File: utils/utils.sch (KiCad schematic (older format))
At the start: 25 parts, among them J1 AIN, J2 BIN, J3 GATE, J4 EURORACK_CONN_10, J5 ~OUT, J6 OUT, J7 Conn_01x04, J8 Conn_01x05, Q1 2N3904, U1 TL072, U2 4066, U3 LM317L_TO92, U4 LM337L_TO92

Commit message: rework PCB
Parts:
- added J9: Conn_01x03_Male, 4ms/4ms-kicad-lib/4ms-footprints.pretty:Pin_Header_Straight_1x03, symbol Connector:Conn_01x03_Male
- added JP1, JP2, JP3, JP4, JP5, JP6, JP7, JP8, JP9: Jumper_2_Open, fruchti/fruchtilib/mod/rcl.pretty:SOLDER_JUMPER_0603_B, symbol Jumper:Jumper_2_Open
- D1: footprint (none) -> 4ms/4ms-kicad-lib/4ms-footprints.pretty:LED-3MM-SQUARE-ANODE
- J7: footprint imciner2/KiCad-Libraries/modules/Connectors.pretty:CONN_2.54mm_1x04 -> imciner2/KiCad-Libraries/modules/Connectors.pretty:CONN_2.54mm_1x05
- Q1: footprint Package_TO_SOT_THT:TO-92_Inline -> 4ms/4ms-kicad-lib/lib-footprints/4ms_Package_TO.pretty:TO-92_OffsetPin2
- R10, R11: footprint (none) -> 4ms/4ms-kicad-lib/4ms-footprints.pretty:Resistor_TH_300
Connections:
- net labels added: STAGE1_OUT
- wire segments 146 -> 172
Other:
- note added: "This is a trick to only use the LED to show gate state\nif the GATE jack is used. When jack is unplugged,\nGATE_CONN is grounded, turning off the transistor.\nWhen jack is plugged, GATE_CONN floats, allowing\nthe gate to control the transistor. R10 gives an input\nimpedance of 100K, since LED is driven by power\nsupply. LED on current depends on GATE but maxes\nabout 4mA"
- note removed: "This is a trick to only use the LED to show gate state\nif the GATE jack is used. When jack is unplugged,\nGATE_CONN is grounded, turning off the transistor.\nWhen jack is plugged, GATE_CONN floats, allowing\nthe gate to control the transistor. R10 gives an input\nimpedance of 100K, since LED is driven by power\nsupply. LED on current about 4mA\n\nTODO: is this enough current? does the slow turn-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"
- moved on the sheet: D1, J7, J8, Q1, R1, R10, R11, R2, R4, R5, U1A, U1B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

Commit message: use through-holes for pot
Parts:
- RV1: footprint rdeterre/misc.pretty:Potentiometer_Bourns_PDB182-K_Dual -> imciner2/KiCad-Libraries/modules/Connectors.pretty:CONN_2.54mm_1x03
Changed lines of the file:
@@
 F 0 "RV1" V 3543 1950 50  0000 C CNN
 F 1 "200K" V 3634 1950 50  0000 C CNN
-F 2 "rdeterre/misc.pretty:Potentiometer_Bourns_PDB182-K_Dual" H 3750 1950 50  0001 C CNN
+F 2 "imciner2/KiCad-Libraries/modules/Connectors.pretty:CONN_2.54mm_1x03" H 3750 1950 50  0001 C CNN
 F 3 "~" H 3750 1950 50  0001 C CNN
 	1    3750 1950

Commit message: add support for fixed CV output when no input
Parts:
- removed RV1: 200K, imciner2/KiCad-Libraries/modules/Connectors.pretty:CONN_2.54mm_1x03, symbol Device:R_POT
- added R12, R3: 10K, 4ms/4ms-kicad-lib/4ms-footprints.pretty:Resistor_TH_300, symbol Device:R
- added RV1: 200K, 4ms/4ms-kicad-lib/4ms-footprints.pretty:Pin_Header_Straight_2x03_Pitch2.54mm, symbol Device:R_POT_Dual_Separate
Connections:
- net labels added: A_CONN
- wire segments 172 -> 178
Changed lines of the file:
@@
 	1    0    0    -1
 $EndComp
-$Comp
-L Device:R R1
-U 1 1 5ECB39F0
-P 2950 2100
-F 0 "R1" V 2743 2100 50  0000 C CNN
-F 1 "100K" V 2834 2100 50  0000 C CNN
-F 2 "4ms/4ms-kicad-lib/4ms-footprints.pretty:Resistor_TH_300" V 2880 2100 50  0001 C CNN
-F 3 "~" H 2950 2100 50  0001 C CNN
-	1    2950 2100
-	0    1    1    0
-$EndComp
-$Comp
-L Device:R R2
-U 1 1 5ECB414F
-P 2950 2400
-F 0 "R2" V 2743 2400 50  0000 C CNN
-F 1 "100K" V 2834 2400 50  0000 C CNN
-F 2 "4ms/4ms-kicad-lib/4ms-footprints.pretty:Resistor_TH_300" V 2880 2400 50  0001 C CNN
-F 3 "~" H 2950 2400 50  0001 C CNN
-	1    2950 2400
-	0    1    1    0
-$EndComp
-$Comp
-L power:GND #PWR05
-U 1 1 5ECB8733
-P 3250 2700
-F 0 "#PWR05" H 3250 2450 50  0001 C CNN
-F 1 "GND" H 3255 2527 50  0000 C CNN
-F 2 "" H 3250 2700 50  0001 C CNN
-F 3 "" H 3250 2700 50  0001 C CNN
-	1    3250 2700
-	1    0    0    -1
-$EndComp
-Wire Wire Line
-	3250 2700 3250 2600
-Wire Wire Line
-	3250 2600 3350 2600
 Wire Wire Line
 	3100 2400 3150 2400
@@
 	900  1550 900  1500
 Wire Wire Line
-	1100 950  1200 950
-Wire Wire Line
-	1200 950  1200 1050
-Wire Wire Line
 	1200 1500 900  1500
 Connection ~ 900  1500
@@
 	900  1500 900  1450
 Wire Wire Line
-	1100 1050 1200 1050
-Connection ~ 1200 1050
-Wire Wire Line
-	1200 1050 1200 1250
-Wire Wire Line
 	1100 1250 1200 1250
-Connection ~ 1200 1250
 Wire Wire Line
 	1200 1250 1200 1500
@@
 	900  2700 900  2650
 Wire Wire Line
-	1100 2100 1200 2100
-Wire Wire Line
-	1200 2100 1200 2200
-Wire Wire Line
 	1200 2650 900  2650
 Connection ~ 900  2650
@@
 	900  2650 900  2600
 Wire Wire Line
-	1100 2200 1200 2200
-Connection ~ 1200 2200
-Wire Wire Line
-	1200 2200 1200 2400
-Wire Wire Line
 	1100 2400 1200 2400
-Connection ~ 1200 2400
 Wire Wire Line
 	1200 2400 1200 2650
@@
 Text Notes 8150 3600 0    50   ~ 0
 The CD4066 has a max power supply voltage of 20V,\nso we step the 24V down to about 19.5 via regulators.\nIn theory we could hacky do this with 6 diodes instead.\n\nBy limiting TL072 to the same supply, we don’t risk over-volting\nthe 4066, because even at rail  outputs the 4066 is safe.
-$Comp
-L Device:R_POT RV1
-U 1 1 5ECB664B
-P 3750 1950
-F 0 "RV1" V 3543 1950 50  0000 C CNN
-F 1 "200K" V 3634 1950 50  0000 C CNN
-F 2 "imciner2/KiCad-Libraries/modules/Connectors.pretty:CONN_2.54mm_1x03" H 3750 1950 50  0001 C CNN
-F 3 "~" H 3750 1950 50  0001 C CNN
-	1    3750 1950
-	0    1    1    0
-$EndComp
 Wire Wire Line
 	3300 1950 3300 2400
@@
 Wire Wire Line
 	8300 5350 8400 5350
+$Comp
+L Device:R_POT_Dual_Separate RV1
+U 2 1 5ED32DF1
+P 3750 1950
+F 0 "RV1" V 3543 1950 50  0000 C CNN
+F 1 "200K" V 3634 1950 50  0000 C CNN
+F 2 "4ms/4ms-kicad-lib/4ms-footprints.pretty:Pin_Header_Straight_2x03_Pitch2.54mm" H 3750 1950 50  0001 C CNN
+F 3 "~" H 3750 1950 50  0001 C CNN
+	2    3750 1950
+	0    1    1    0
+$EndComp
+$Comp
+L Device:R_POT_Dual_Separate RV1
+U 1 1 5ED34631
+P 2800 3400
+F 0 "RV1" H 2731 3446 50  0000 R CNN
+F 1 "200K" H 2731 3355 50  0000 R CNN
+F 2 "4ms/4ms-kicad-lib/4ms-footprints.pretty:Pin_Header_Straight_2x03_Pitch2.54mm" H 2800 3400 50  0001 C CNN
+F 3 "~" H 2800 3400 50  0001 C CNN
+	1    2800 3400
+	1    0    0    -1
+$EndComp
+$Comp
+L Device:R R2
+U 1 1 5ECB414F
+P 2950 2400
+F 0 "R2" V 2743 2400 50  0000 C CNN
+F 1 "100K" V 2834 2400 50  0000 C CNN
+F 2 "4ms/4ms-kicad-lib/4ms-footprints.pretty:Resistor_TH_300" V 2880 2400 50  0001 C CNN
+F 3 "~" H 2950 2400 50  0001 C CNN
+	1    2950 2400
+	0    1    1    0
+$EndComp
+$Comp
+L Device:R R1
+U 1 1 5ECB39F0
+P 2950 2100
+F 0 "R1" V 2743 2100 50  0000 C CNN
+F 1 "100K" V 2834 2100 50  0000 C CNN
+F 2 "4ms/4ms-kicad-lib/4ms-footprints.pretty:Resistor_TH_300" V 2880 2100 50  0001 C CNN
+F 3 "~" H 2950 2100 50  0001 C CNN
+	1    2950 2100
+	0    1    1    0
+$EndComp
+$Comp
+L power:+10V #PWR0101
+U 1 1 5ED62298
+P 2800 2800
+F 0 "#PWR0101" H 2800 2650 50  0001 C CNN
+F 1 "+10V" H 2815 2973 50  0000 C CNN
+F 2 "" H 2800 2800 50  0001 C CNN
+F 3 "" H 2800 2800 50  0001 C CNN
+	1    2800 2800
+	1    0    0    -1
+$EndComp
+$Comp
+L power:-10V #PWR0102
+U 1 1 5EDA3B1B
+P 2800 4000
+F 0 "#PWR0102" H 2800 4100 50  0001 C CNN
+F 1 "-10V" H 2815 4173 50  0000 C CNN
+F 2 "" H 2800 4000 50  0001 C CNN
+F 3 "" H 2800 4000 50  0001 C CNN
+	1    2800 4000
+	-1   0    0    1
+$EndComp
+Wire Wire Line
+	2950 3400 3100 3400
+Wire Wire Line
+	3100 3400 3100 2600
+Wire Wire Line
+	3100 2600 3350 2600
+Wire Wire Line
+	2800 2800 2800 2900
+Wire Wire Line
+	2800 3250 2800 3200
+$Comp
+L Device:R R3
+U 1 1 5ED35BE2
+P 2800 3050
+F 0 "R3" V 2593 3050 50  0000 C CNN
+F 1 "10K" V 2684 3050 50  0000 C CNN
+F 2 "4ms/4ms-kicad-lib/4ms-footprints.pretty:Resistor_TH_300" V 2730 3050 50  0001 C CNN
+F 3 "~" H 2800 3050 50  0001 C CNN
+	1    2800 3050
+	-1   0    0    1
+$EndComp
+Wire Wire Line
+	2800 4000 2800 3900
+Wire Wire Line
+	2800 3600 2800 3550
+$Comp
+L Device:R R12
+U 1 1 5ED360F9
+P 2800 3750
+F 0 "R12" V 2593 3750 50  0000 C CNN
+F 1 "10K" V 2684 3750 50  0000 C CNN
+F 2 "4ms/4ms-kicad-lib/4ms-footprints.pretty:Resistor_TH_300" V 2730 3750 50  0001 C CNN
+F 3 "~" H 2800 3750 50  0001 C CNN
+	1    2800 3750
+	-1   0    0    1
+$EndComp
+Wire Wire Line
+	1100 2100 1200 2100
+Wire Wire Line
+	1100 2200 1200 2200
+Wire Wire Line
+	1200 2100 1200 2200
+Connection ~ 1200 2400
+Connection ~ 1200 2200
+Wire Wire Line
+	1200 2200 1200 2400
+Text GLabel 1450 950  2    50   Input ~ 0
+A_CONN
+Wire Wire Line
+	1450 950  1200 950
+Text GLabel 3250 3400 2    50   Input ~ 0
+A_CONN
+Wire Wire Line
+	3250 3400 3100 3400
+Connection ~ 3100 3400
+Wire Wire Line
+	1100 1050 1200 1050
+Wire Wire Line
+	1200 1050 1200 950
+Connection ~ 1200 950
+Wire Wire Line
+	1200 950  1100 950
 $EndSCHEMATC

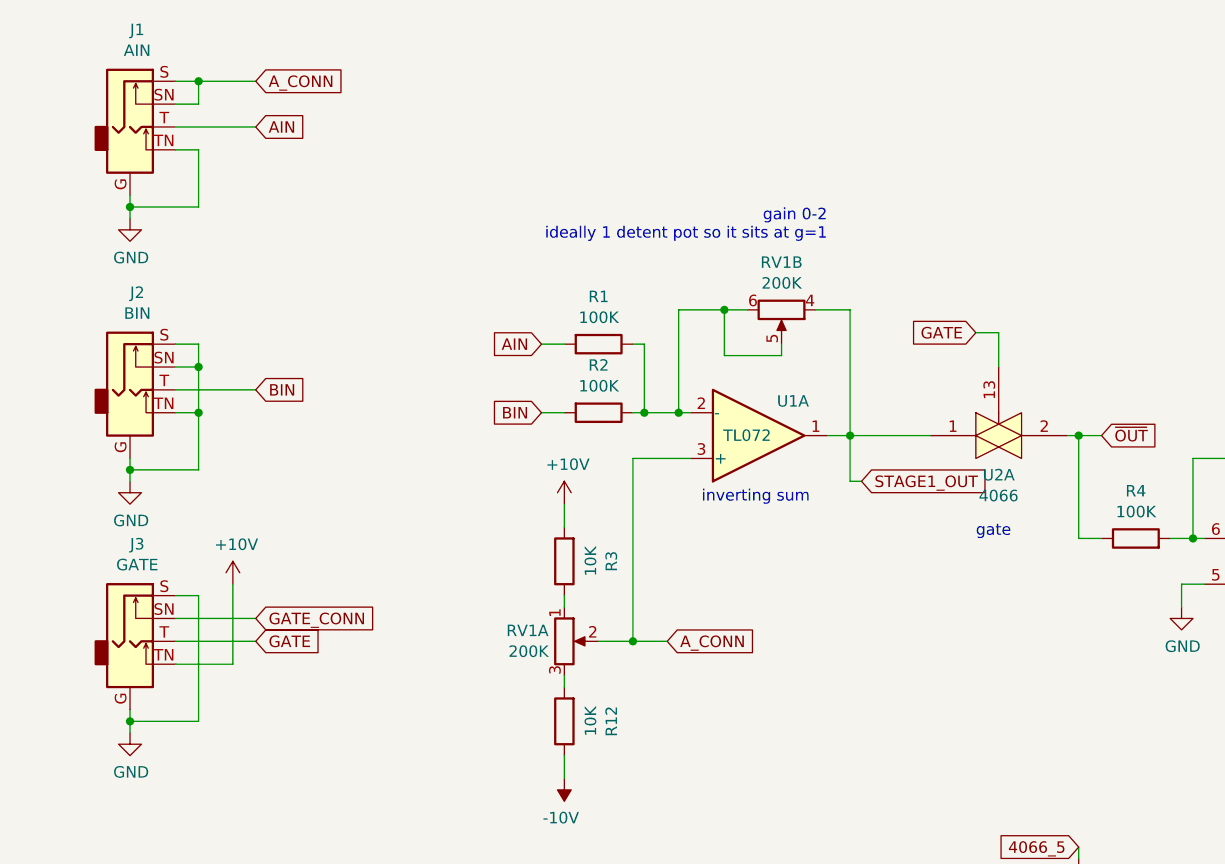
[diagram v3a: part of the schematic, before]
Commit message: correction based on breadboard test
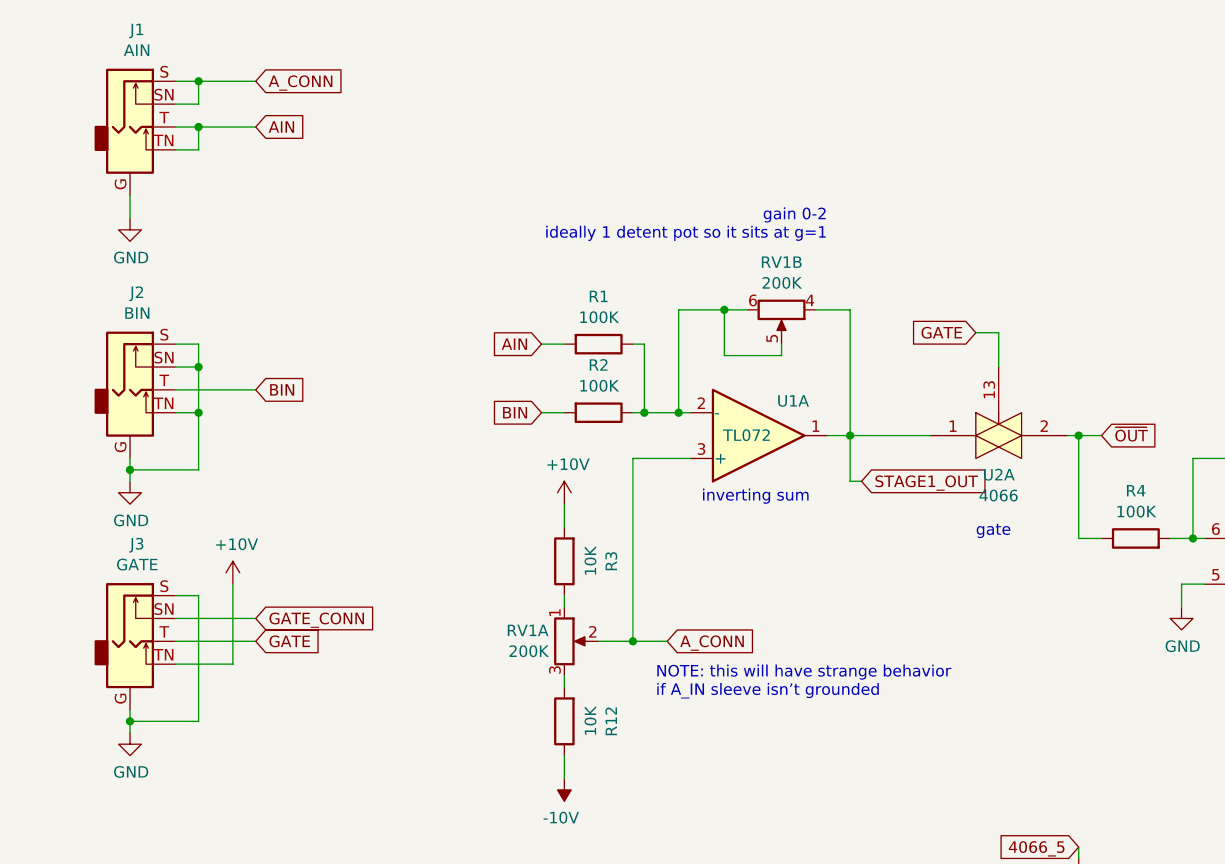
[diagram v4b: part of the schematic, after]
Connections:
- net AIN: now also J1.TN
- net GND: no longer J1.TN
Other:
- note added: "NOTE: this will have strange behavior\nif A_IN sleeve isn’t grounded"
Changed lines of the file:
@@
 	1    0    0    -1
 $EndComp
-Wire Wire Line
-	900  1550 900  1500
-Wire Wire Line
-	1200 1500 900  1500
-Connection ~ 900  1500
-Wire Wire Line
-	900  1500 900  1450
-Wire Wire Line
-	1100 1250 1200 1250
-Wire Wire Line
-	1200 1250 1200 1500
 Text GLabel 1450 1150 2    50   Input ~ 0
 AIN
 Wire Wire Line
-	1450 1150 1100 1150
+	1450 1150 1200 1150
 $Comp
 L synth:AudioJack2_Ground_Switch J2
@@
 Wire Wire Line
 	1200 950  1100 950
+Wire Wire Line
+	900  1450 900  1550
+Wire Wire Line
+	1100 1250 1200 1250
+Wire Wire Line
+	1200 1250 1200 1150
+Connection ~ 1200 1150
+Wire Wire Line
+	1200 1150 1100 1150
+Text Notes 3200 3650 0    50   ~ 0
+NOTE: this will have strange behavior\nif A_IN sleeve isn’t grounded
 $EndSCHEMATC

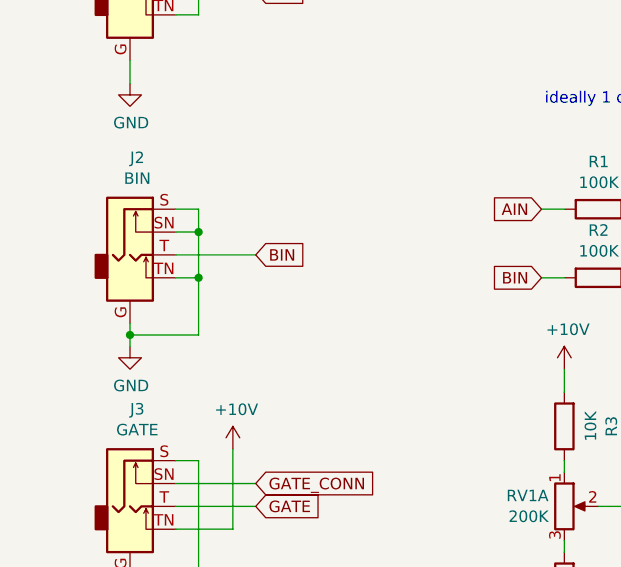
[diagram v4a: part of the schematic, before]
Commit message: correct ground issue
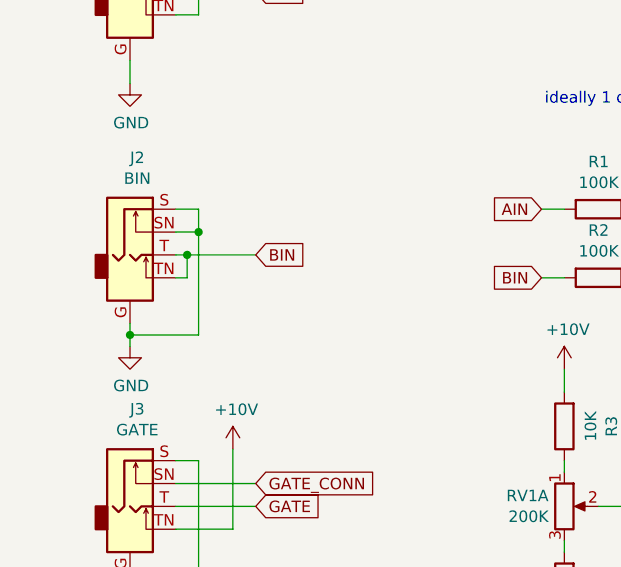
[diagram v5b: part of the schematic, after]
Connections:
- net BIN: now also J2.TN
- net GND: no longer J2.TN
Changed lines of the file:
@@
 Wire Wire Line
 	900  2650 900  2600
-Wire Wire Line
-	1100 2400 1200 2400
-Wire Wire Line
-	1200 2400 1200 2650
 Text GLabel 1450 2300 2    50   Input ~ 0
 BIN
 Wire Wire Line
-	1450 2300 1100 2300
+	1450 2300 1150 2300
 $Comp
 L synth:AudioJack2_Ground_Switch J3
@@
 Wire Wire Line
 	1200 2100 1200 2200
-Connection ~ 1200 2400
 Connection ~ 1200 2200
-Wire Wire Line
-	1200 2200 1200 2400
 Text GLabel 1450 950  2    50   Input ~ 0
 A_CONN
@@
 Text Notes 3200 3650 0    50   ~ 0
 NOTE: this will have strange behavior\nif A_IN sleeve isn’t grounded
+Wire Wire Line
+	1200 2200 1200 2650
+Wire Wire Line
+	1100 2400 1150 2400
+Wire Wire Line
+	1150 2400 1150 2300
+Connection ~ 1150 2300
+Wire Wire Line
+	1150 2300 1100 2300
 $EndSCHEMATC

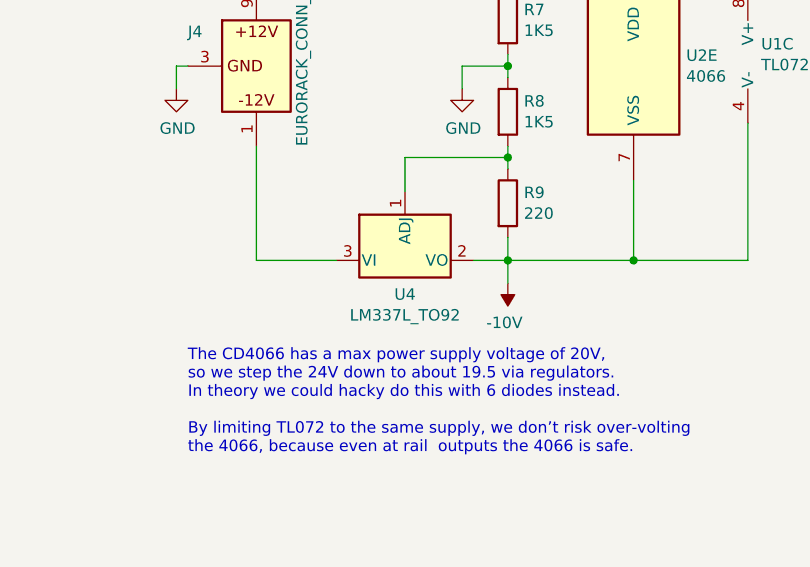
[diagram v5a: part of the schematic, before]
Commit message: fix some bugs in the circuit
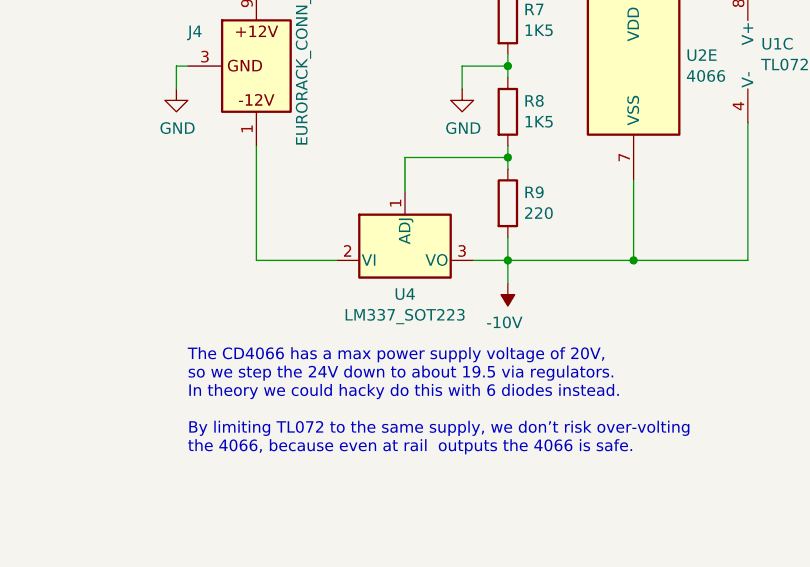
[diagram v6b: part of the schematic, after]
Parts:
- removed U4: LM337L_TO92, KiCad/TO_SOT_Packages_THT.pretty:TO-220-3_Vertical, symbol Regulator_Linear:LM337L_TO92
- added U4: LM337_SOT223, KiCad/TO_SOT_Packages_THT.pretty:TO-220-3_Vertical, symbol Regulator_Linear:LM337_SOT223
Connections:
- net -10V: now also U4.3 (VO)
- net at J4.1 (12V_N): now also U4.2 (VI)
- net at R8.2, R9.1: now also U4.1 (ADJ)
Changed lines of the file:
@@
-$EndComp
-$Comp
-L Regulator_Linear:LM337L_TO92 U4
-U 1 1 5EE7ED7D
-P 9100 2750
-F 0 "U4" H 9100 2601 50  0000 C CNN
-F 1 "LM337L_TO92" H 9100 2510 50  0000 C CNN
-F 2 "KiCad/TO_SOT_Packages_THT.pretty:TO-220-3_Vertical" H 9100 2550 50  0001 C CIN
-F 3 "http://www.ti.com/lit/ds/symlink/lm337l.pdf" H 9100 2750 50  0001 C CNN
-	1    9100 2750
-	1    0    0    -1
 $EndComp
 $Comp
@@
 Wire Wire Line
 	1150 2300 1100 2300
+$Comp
+L Regulator_Linear:LM337_SOT223 U4
+U 1 1 5ED777C2
+P 9100 2750
+F 0 "U4" H 9100 2601 50  0000 C CNN
+F 1 "LM337_SOT223" H 9100 2510 50  0000 C CNN
+F 2 "KiCad/TO_SOT_Packages_THT.pretty:TO-220-3_Vertical" H 9100 2550 50  0001 C CIN
+F 3 "http://www.ti.com/lit/ds/symlink/lm337-n.pdf" H 9100 2750 50  0001 C CNN
+	1    9100 2750
+	1    0    0    -1
+$EndComp
 $EndSCHEMATC
